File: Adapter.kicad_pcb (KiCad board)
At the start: 6 copper layers, 189.7 x 92 mm, 291 parts, among them J1 GD820HTX75P6HB, J2 2-338069-0, U1 R-78E3.3-1.0, U10 74LVC1G04, U11 LMV7219M5, U2 LM1117GS-3.3, U4 74LVC1G04, U5 ADuM1200AR, U6 74LVC1G04, U7 74LVC1G04, U8 74LVC1G04, U9 74LVC1G04

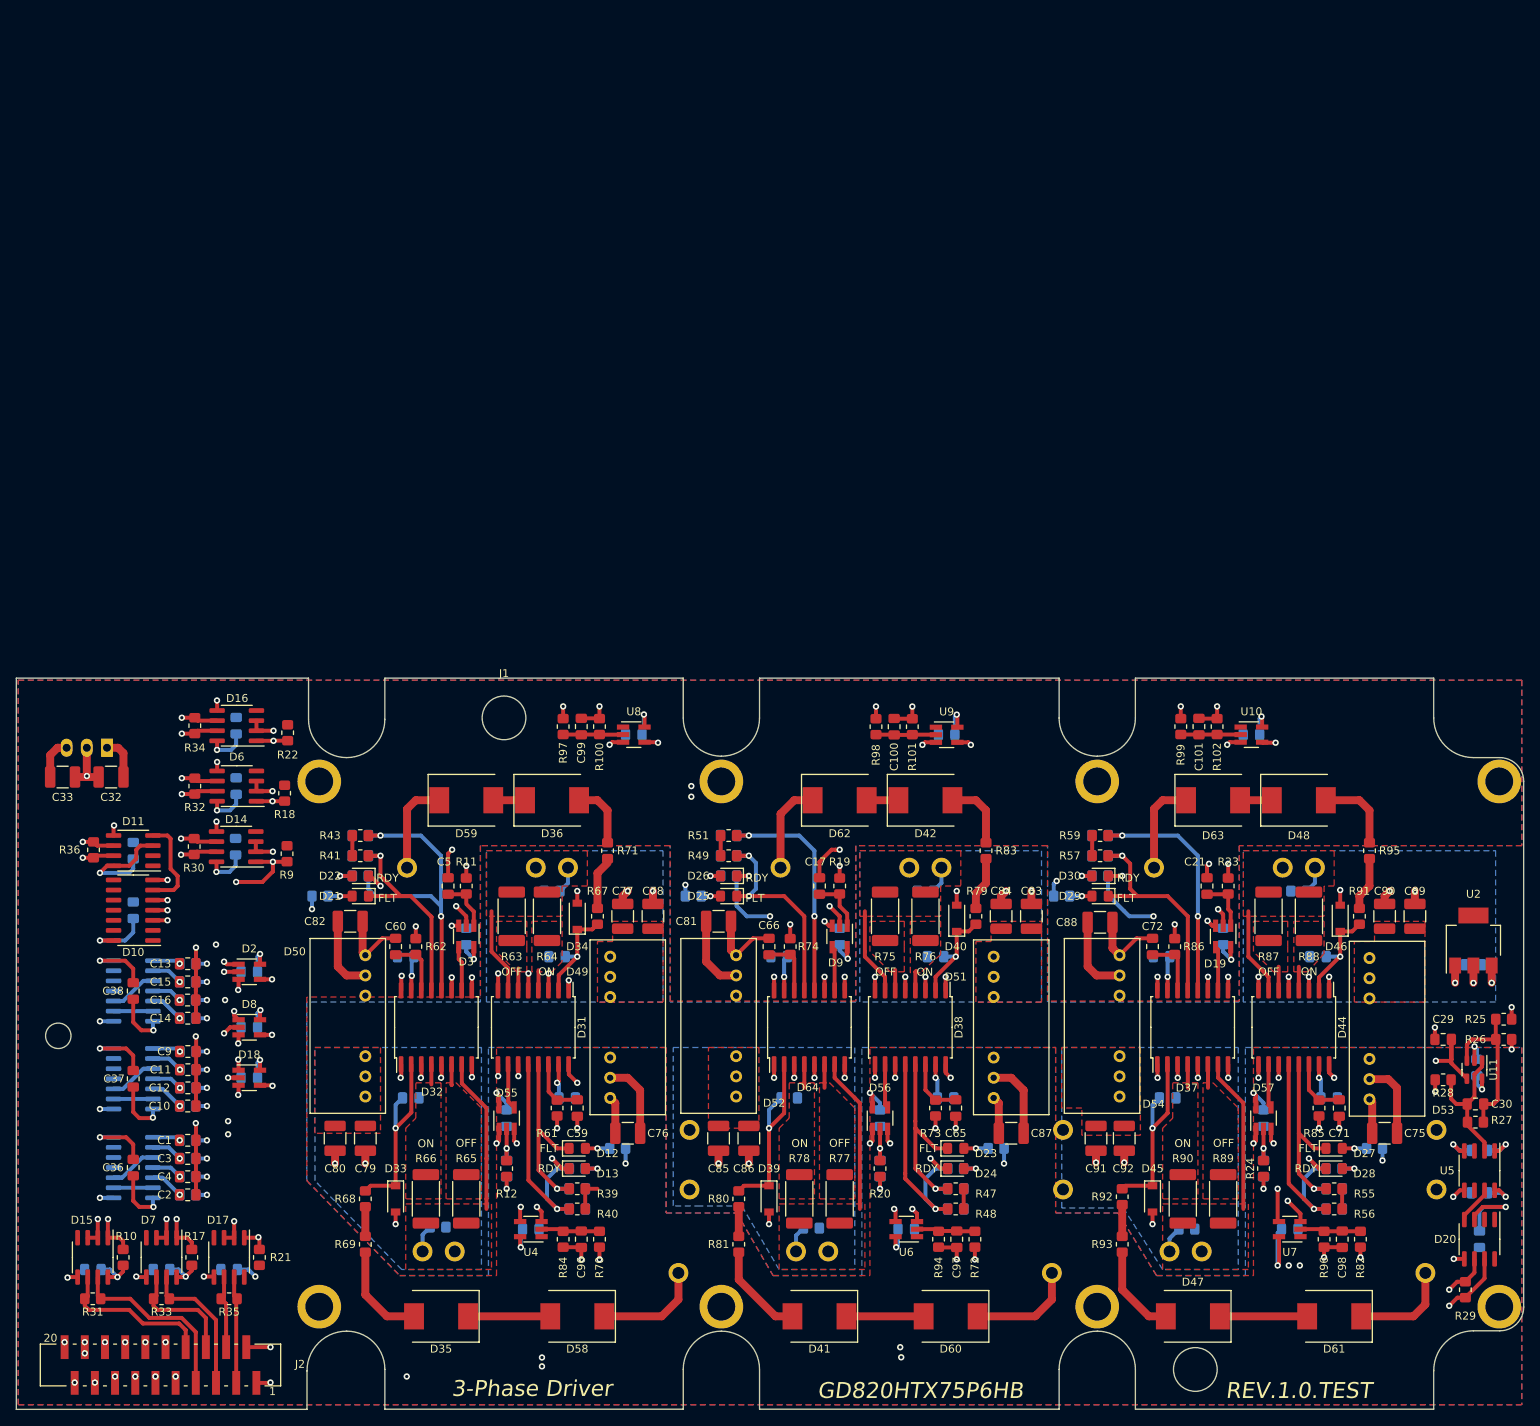
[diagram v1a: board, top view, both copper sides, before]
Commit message: Изменил схему
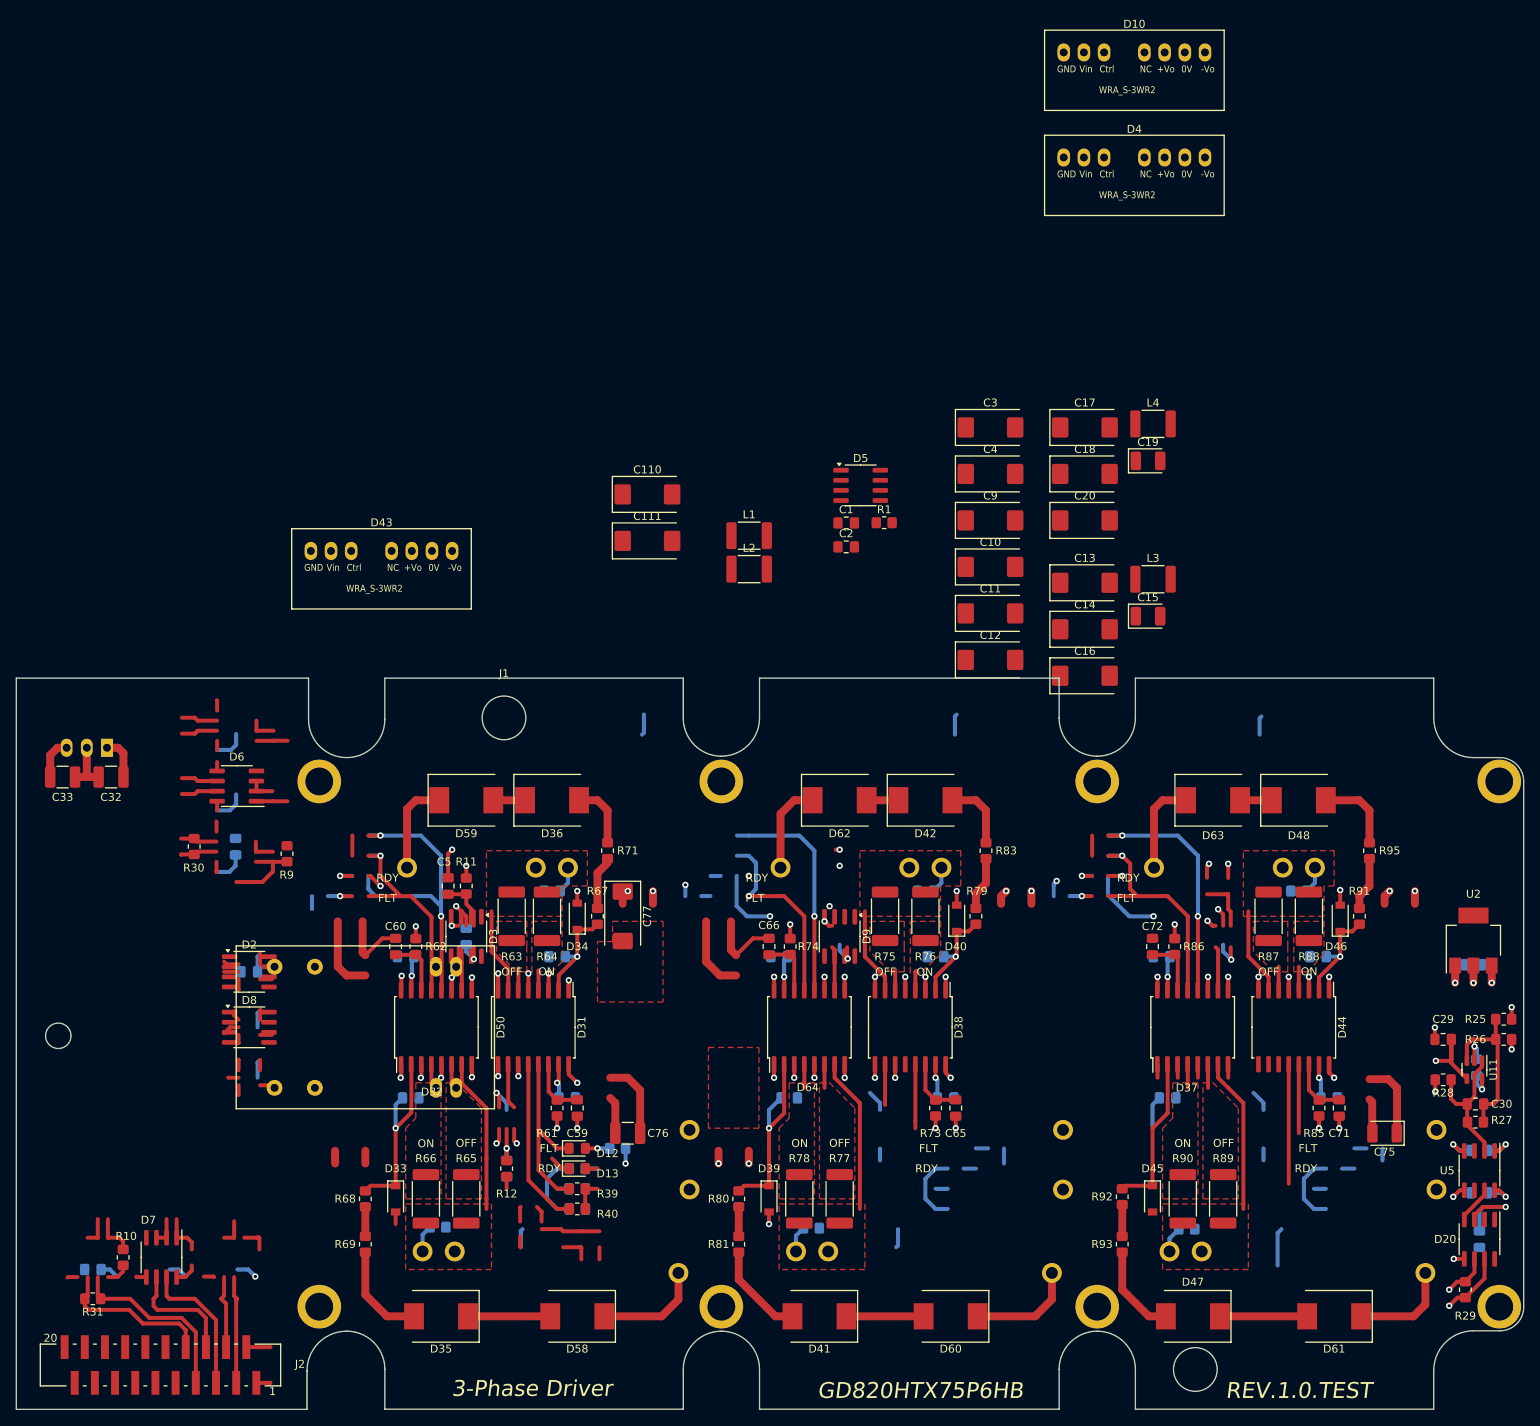
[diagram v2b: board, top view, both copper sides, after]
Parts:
- removed C100, C101, C21, C22, C47, C48, C49, C50, C51, C52, C53, C54, C55, C56, C96, C97, C98, C99: 56p, Capacitor_SMD:C_0805_2012Metric_Pad1.18x1.45mm_HandSolder
- removed C102, C103, C104, C105, C106, C107, C23, C24, C25, C26, C31, C36, C37, C38, C39, C43, C44, C93, C94, C95: 2.2u, Capacitor_SMD:C_0805_2012Metric_Pad1.18x1.45mm_HandSolder
- removed C78, C79, C80, C81, C82, C83, C84, C85, C86, C87, C88, C89, C90, C91, C92: 10u, Capacitor_SMD:C_1210_3225Metric_Pad1.33x2.70mm_HandSolder
- removed D1: SN74AC08DR, Package_SO:SOIC-14_3.9x8.7mm_P1.27mm
- removed D11, D14, D15, D16, D17: ADM3485E, Package_SO:SOIC-8_3.9x4.9mm_P1.27mm
- removed D18: SN74AHC1G32DBVR, Package_TO_SOT_SMD:SOT-23-5_HandSoldering
- removed D19, D55, D56, D57: SN74AHC1G86DBVR, Package_TO_SOT_SMD:SOT-23-5_HandSoldering
- removed D21, D23, D25, D27, D29: FLT, LED_SMD:LED_0805_2012Metric_Pad1.15x1.40mm_HandSolder
- removed D22, D24, D26, D28, D30: RDY, LED_SMD:LED_0805_2012Metric_Pad1.15x1.40mm_HandSolder
- removed D49, D51, D52, D53, D54: WRA1215S-3WR2, Mornsun:WRA1215S-3WR2
- removed R100, R101, R102, R17, R18, R21, R22, R41, R47, R49, R55, R57, R84, R94, R96: 10k, Resistor_SMD:R_0805_2012Metric_Pad1.20x1.40mm_HandSolder
- removed R13, R14, R15, R16, R19, R2, R20, R23, R24, R3, R32, R33, R34, R35, R36, R4, R43, R48, R5, R51, R56, R59, R6, R7, R70, R72, R8, R82, R97, R98, R99: 120, Resistor_SMD:R_0805_2012Metric_Pad1.20x1.40mm_HandSolder
- removed R42, R44, R45, R46, R50, R52, R53, R54, R58, R60: 330, Resistor_SMD:R_0805_2012Metric_Pad1.20x1.40mm_HandSolder
- removed U10, U4, U6, U7, U8, U9: 74LVC1G04, Package_TO_SOT_SMD:SOT-23-5_HandSoldering
- added C110: 10u, Capacitor_Tantalum_SMD:CP_EIA-7343-31_Kemet-D, F.Cu at (118.0, 24.4)
- added C111: 47u, Capacitor_Tantalum_SMD:CP_EIA-7343-31_Kemet-D, F.Cu at (118.0, 30.2)
- added D43: WRA1215S-3WR2, Mornsun:WRA_S-3WR2, F.Cu at (84.6, 31.5)
- added L1: 4.7u, Inductor_SMD:L_1812_4532Metric_Pad1.30x3.40mm_HandSolder, F.Cu at (130.8, 29.6)
- added L2: 4.7u, Inductor_SMD:L_1812_4532Metric_Pad1.30x3.40mm_HandSolder, F.Cu at (130.8, 33.8)
- added L3: 4.7u, Inductor_SMD:L_1812_4532Metric_Pad1.30x3.40mm_HandSolder, F.Cu at (181.7, 35.1)
- added L4: 4.7u, Inductor_SMD:L_1812_4532Metric_Pad1.30x3.40mm_HandSolder, F.Cu at (181.7, 15.5)
- C1, C2, C5, C6: value 56p -> 2.2u
- C10, C11, C12, C13, C16, C17, C3, C4, C9: value 56p -> 47u; footprint Capacitor_SMD:C_0805_2012Metric_Pad1.18x1.45mm_HandSolder -> Capacitor_Tantalum_SMD:CP_EIA-7343-31_Kemet-D
- C14: value 56p -> 10u; footprint Capacitor_SMD:C_0805_2012Metric_Pad1.18x1.45mm_HandSolder -> Capacitor_Tantalum_SMD:CP_EIA-7343-31_Kemet-D
- C15: value 56p -> 1u; footprint Capacitor_SMD:C_0805_2012Metric_Pad1.18x1.45mm_HandSolder -> Capacitor_Tantalum_SMD:CP_EIA-3528-21_Kemet-B
- C18: value 56p -> 10u; footprint Capacitor_SMD:C_0805_2012Metric_Pad1.18x1.45mm_HandSolder -> Capacitor_Tantalum_SMD:CP_EIA-7343-31_Kemet-D; moved to F.Cu
- C19: value 2.2u -> 1u; footprint Capacitor_SMD:C_0805_2012Metric_Pad1.18x1.45mm_HandSolder -> Capacitor_Tantalum_SMD:CP_EIA-3528-21_Kemet-B; moved to F.Cu
- C20: value 2.2u -> 47u; footprint Capacitor_SMD:C_0805_2012Metric_Pad1.18x1.45mm_HandSolder -> Capacitor_Tantalum_SMD:CP_EIA-7343-31_Kemet-D; moved to F.Cu
- C75: value 10u -> 1u; footprint Capacitor_SMD:C_1210_3225Metric_Pad1.33x2.70mm_HandSolder -> Capacitor_Tantalum_SMD:CP_EIA-3528-21_Kemet-B
- C76: value 10u -> 1u
- C77: value 10u -> 47u; footprint Capacitor_SMD:C_1210_3225Metric_Pad1.33x2.70mm_HandSolder -> Capacitor_Tantalum_SMD:CP_EIA-7343-31_Kemet-D
- D10: value SN74HC11DR -> WRA1215S-3WR2; footprint Package_SO:SOIC-14_3.9x8.7mm_P1.27mm -> Mornsun:WRA_S-3WR2
- D2, D8: value SN74AHC1G32DBVR -> ADM3485E; footprint Package_TO_SOT_SMD:SOT-23-5_HandSoldering -> Package_SO:SOIC-8_3.9x4.9mm_P1.27mm
- D3, D9: value SN74AHC1G86DBVR -> ADM3485E; footprint Package_TO_SOT_SMD:SOT-23-5_HandSoldering -> Package_SO:SOIC-8_3.9x4.9mm_P1.27mm
- D4: value SN74AC08DR -> WRA1215S-3WR2; footprint Package_SO:SOIC-14_3.9x8.7mm_P1.27mm -> Mornsun:WRA_S-3WR2; moved to F.Cu
- D5: value SN74AC08DR -> ADM3485E; footprint Package_SO:SOIC-14_3.9x8.7mm_P1.27mm -> Package_SO:SOIC-8_3.9x4.9mm_P1.27mm; moved to F.Cu
- D50: value WRA1215S-3WR2 -> URA2415ZP-6WR3; footprint Mornsun:WRA1215S-3WR2 -> Mornsun:URA_ZP-6WR3
- R1: moved to F.Cu
- R10, R9: value 10k -> 120
- R39: value 10k -> 30k
- R40: value 120 -> 30k
- moved D4 171.2 mm to (179.3, -18.0), turned to 0 degrees
- moved D10 165.9 mm to (179.3, -31.2), turned to 0 degrees
- moved C3 136.6 mm to (161.2, 16.0)
- moved C4 134.3 mm to (161.2, 21.8)
- moved C15 129.3 mm to (181.0, 39.7)
- moved C14 123.1 mm to (173.1, 41.4)
- moved C20 123.0 mm to (173.1, 27.7), turned to 0 degrees
- moved C13 122.7 mm to (173.1, 35.5)
- moved C10 121.7 mm to (161.2, 33.5)
- moved C9 121.1 mm to (161.2, 27.7)
- moved C16 120.1 mm to (173.1, 47.2)
- moved R1 117.1 mm to (147.8, 27.9)
- moved C2 116.3 mm to (143.1, 31.0)
- moved C11 116.2 mm to (161.2, 39.4)
- moved C12 114.5 mm to (161.2, 45.2)
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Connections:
- C1 pad 1: Net-(D1-1A) -> +3V3
- C10 pad 1: Net-(D4-2B) -> E4
- C10 pad 2: GND -> -15V_L1
- C11 pad 1: Net-(D4-1B) -> +15V_L1
- C11 pad 2: GND -> E6
- C12 pad 1: Net-(D4-2A) -> E6
- C12 pad 2: GND -> -15V_L1
- C13 pad 1: Net-(D5-1A) -> +15V_H2
- C13 pad 2: GND -> E3
- C14 pad 1: Net-(D5-2B) -> +15V
- C15 pad 1: Net-(D5-1B) -> Net-(D4-Vin)
- C16 pad 1: Net-(D5-2A) -> E3
- C16 pad 2: GND -> -15V_H2
- C17 pad 1: Net-(D9-A) -> +15V_H3
- C17 pad 2: GND -> E5
- C18 pad 1: Net-(D56-B) -> +15V
- C19 pad 1: +3V3 -> Net-(D10-Vin)
- C2 pad 1: Net-(D1-2B) -> +3V3
- C20 pad 1: +3V3 -> E5
- C20 pad 2: GND -> -15V_H3
- C27 pad 2: -15V_L3 -> -15V_L1
- C28 pad 2: -15V_L3 -> -15V_L1
- C29 pad 2: -15V_L3 -> -15V_L1
- C3 pad 1: Net-(D1-1B) -> +15V_L1
- C3 pad 2: GND -> E2
- C4 pad 1: Net-(D1-2A) -> E2
- C4 pad 2: GND -> -15V_L1
- C40 pad 2: -15V_L3 -> -15V_L1
- C45 pad 1: FLT_L1 -> FLT
- C46 pad 1: RDY_L1 -> RDY
- C5 pad 1: Net-(D3-A) -> +3V3
- C6 pad 1: Net-(D55-B) -> +3V3
- C75 pad 1: +15V -> Net-(D43-Vin)
- C77 pad 1: +15V_L1 -> E1
- C77 pad 2: E2 -> -15V_H1
- C9 pad 1: Net-(D4-1A) -> +15V_L1
- C9 pad 2: GND -> E4
- D10 pad 1: unconnected-(D10-1A-Pad1) -> GND
- D10 pad 2: unconnected-(D10-1B-Pad2) -> Net-(D10-Vin)
- D10 pad 3: FAULT_1 -> unconnected-(D10-Ctrl-Pad3)
- D10 pad 5: FAULT_3 -> (no net)
- D10 pad 6: FAULT_COMM -> +15V_H3
- D10 pad 7: GND -> E5
- D10 pad 8: unconnected-(D10-3Y-Pad8) -> -15V_H3
- D12 pad 1: FLT_L1 -> FLT
- D2 pad 1: Net-(D14-RO) -> PWM_H1
- D2 pad 2: Net-(D15-RO) -> GND
- D2 pad 4: Net-(D2-Y) -> unconnected-(D2-DI-Pad4)
- D2 pad 5: +3V3 -> GND
- D3 pad 1: Net-(D3-A) -> PWM_L1
- D3 pad 2: Net-(D2-Y) -> GND
- D3 pad 4: PWM_H1 -> unconnected-(D3-DI-Pad4)
- D3 pad 5: +3V3 -> GND
- D31 pad 11: GND -> PWM_H1
- D32 pad 11: GND -> PWM_L1
- D37 pad 11: GND -> PWM_L3
- D38 pad 1: -15V_L2 -> -15V_L1
- D38 pad 11: GND -> PWM_H2
- D38 pad 5: +15V_L2 -> +15V_L1
- D38 pad 8: -15V_L2 -> -15V_L1
- D4 pad 1: Net-(D4-1A) -> GND
- D4 pad 2: Net-(D4-1B) -> Net-(D4-Vin)
- D4 pad 3: /Fault2/FLT -> unconnected-(D4-Ctrl-Pad3)
- D4 pad 5: Net-(D4-2B) -> (no net)
- D4 pad 6: /Fault2/RDY -> +15V_H2
- D4 pad 7: GND -> E3
- D4 pad 8: FAULT_2 -> -15V_H2
- D44 pad 1: -15V_L3 -> -15V_L1
- D44 pad 11: GND -> PWM_H3
- D44 pad 5: +15V_L3 -> +15V_L1
- D44 pad 8: -15V_L3 -> -15V_L1
- D5 pad 1: Net-(D5-1A) -> unconnected-(D5-RO-Pad1)
- D5 pad 2: Net-(D5-1B) -> +3V3
- D5 pad 3: /Fault3/FLT -> +3V3
- D5 pad 4: Net-(D5-2A) -> Net-(D1-Y)
- D5 pad 5: Net-(D5-2B) -> GND
- D5 pad 6: /Fault3/RDY -> ERR_P
- D5 pad 7: GND -> ERR_N
- D5 pad 8: FAULT_3 -> +3V3
- D50 pad 2: +15V -> GND
- D50 pad 3: unconnected-(D50-Ctrl-Pad3) -> GND
- D6 pad 1: Net-(D6-RO) -> PWM_L3
- D6 pad 6: PWM2_L_P -> PWM3_L_P
- D6 pad 7: PWM2_L_N -> PWM3_L_N
- D64 pad 11: GND -> PWM_L2
- D7 pad 1: Net-(D7-RO) -> PWM_H3
- D7 pad 6: PWM2_H_P -> PWM3_H_P
- D7 pad 7: PWM2_H_N -> PWM3_H_N
- D8 pad 1: Net-(D6-RO) -> PWM_L2
- D8 pad 2: Net-(D7-RO) -> GND
- D8 pad 4: Net-(D56-A) -> unconnected-(D8-DI-Pad4)
- D8 pad 5: +3V3 -> GND
- D9 pad 1: Net-(D9-A) -> PWM_H2
- D9 pad 2: Net-(D56-A) -> GND
- D9 pad 4: PWM_H2 -> unconnected-(D9-DI-Pad4)
- D9 pad 5: +3V3 -> GND
- J2 pad 20: Reset -> unconnected-(J2-Pad20)
- R1 pad 1: Net-(D1-1A) -> ERR_N
- R1 pad 2: FLT_H1 -> ERR_P
- R10 pad 1: +3V3 -> PWM2_H_N
- R10 pad 2: Net-(D15-RO) -> PWM2_H_P
- R11 pad 1: Net-(D14-RO) -> PWM3_L_N
- R11 pad 2: Net-(D3-A) -> PWM3_L_P
- R12 pad 1: Net-(D15-RO) -> PWM3_H_N
- R12 pad 2: Net-(D55-B) -> PWM3_H_P
- R26 pad 1: -15V_L3 -> -15V_L1
- R38 pad 2: RDY_L1 -> RDY
- R39 pad 1: FLT_L1 -> FLT
- R40 pad 1: RDY_L1 -> RDY
- R61 pad 1: RST_L1 -> PWM_L1
- R62 pad 1: RST_H1 -> PWM_H1
- R73 pad 1: RST_L2 -> PWM_L2
- R74 pad 1: RST_H2 -> PWM_H2
- R85 pad 1: RST_L3 -> PWM_L3
- R86 pad 1: RST_H3 -> PWM_H3
- R9 pad 1: +3V3 -> PWM2_L_N
- R9 pad 2: Net-(D14-RO) -> PWM2_L_P
- U11 pad 2: -15V_L3 -> -15V_L1
- U2 pad 1: -15V_L3 -> -15V_L1
- U5 pad 4: -15V_L3 -> -15V_L1
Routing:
- net (no net): track 0.00 -> 657.1 mm, vias 0 -> 9
- net Reset: track 413.3 -> 0.00 mm, vias 7 -> 0
- net unconnected-(J2-Pad20): track 0.00 -> 405.8 mm
- net Net-(D18-Y): track 348.2 -> 0.00 mm, vias 3 -> 0
- net Net-(D56-A): track 223.4 -> 0.00 mm, vias 3 -> 0
- net Net-(D17-RO): track 177.7 -> 0.00 mm, vias 3 -> 0
- net Net-(D16-RO): track 177.4 -> 0.00 mm, vias 3 -> 0
- net Net-(D7-RO): track 152.9 -> 0.00 mm, vias 3 -> 0
- net PWM2_L_P: track 82.6 -> 228.7 mm, vias 2 -> 1
- net Net-(D6-RO): track 114.1 -> 0.00 mm, vias 3 -> 0
- net GND: track 239.9 -> 129.4 mm, vias 76 -> 26
- net Net-(D2-Y): track 109.9 -> 0.00 mm, vias 3 -> 0
- net Net-(D15-RO): track 107.2 -> 0.00 mm, vias 3 -> 0
- net PWM3_H_N: track 13.5 -> 113.4 mm
- net PWM_L3: track 5.56 -> 95.9 mm, vias 0 -> 3
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- added copper zone on In2.Cu, net -15V_L1
- removed copper zone on In1.Cu, net +15V
- removed copper zone on In3.Cu, net +15V_H1
- removed copper zone on In3.Cu, net +15V_H2
- removed copper zone on In3.Cu, net +15V_H3
- removed copper zone on In3.Cu, net +15V_L1
- removed copper zone on In3.Cu, net +15V_L2
- removed copper zone on In3.Cu, net +15V_L3
- removed copper zone on F.Cu, net +3V3
- removed copper zone on In4.Cu, net -15V_H1
- removed copper zone on In4.Cu, net -15V_H2
- removed copper zone on In4.Cu, net -15V_H3
- removed copper zone on In4.Cu, net -15V_L1
- removed copper zone on In4.Cu, net -15V_L2
- removed copper zone on In2.Cu, net -15V_L3
- removed copper zone on In4.Cu, net -15V_L3
- removed copper zone on B.Cu, net E1
- removed copper zone on F.Cu, net E1
- removed copper zone on B.Cu, net E2
- removed copper zone on B.Cu, net E3
- removed copper zone on B.Cu, net E4
- removed copper zone on F.Cu, net E4
- removed copper zone on B.Cu, net E5
- removed copper zone on F.Cu, net E5
- removed copper zone on B.Cu, net E6
- removed copper zone on F.Cu, net E6
- removed copper zone on B.Cu, net GND

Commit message: Разместил все три стойки в своей области
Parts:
- removed C110: 10u, Capacitor_Tantalum_SMD:CP_EIA-7343-31_Kemet-D
- removed C111, C77: 47u, Capacitor_Tantalum_SMD:CP_EIA-7343-31_Kemet-D
- removed C75: 1u, Capacitor_Tantalum_SMD:CP_EIA-3528-21_Kemet-B
- removed C76: 1u, Capacitor_SMD:C_1210_3225Metric_Pad1.33x2.70mm_HandSolder
- removed D50: URA2415ZP-6WR3, Mornsun:URA_ZP-6WR3
- removed H1: MountingHole, MountingHole:MountingHole_3.2mm_M3
- removed R63, R64, R65, R75, R76, R77, R78, R87, R88, R89, R90: 3, Resistor_SMD:R_2512_6332Metric_Pad1.40x3.35mm_HandSolder
- added C21: 0.1u, Capacitor_SMD:C_0805_2012Metric_Pad1.18x1.45mm_HandSolder, F.Cu at (-4.57, 68.0)
- added C22: 10u, Capacitor_SMD:C_0805_2012Metric_Pad1.18x1.45mm_HandSolder, F.Cu at (-4.57, 71.0)
- added C23: 0.1u, Capacitor_SMD:C_0805_2012Metric_Pad1.18x1.45mm_HandSolder, F.Cu at (-4.57, 74.0)
- added C24: 10u, Capacitor_SMD:C_0805_2012Metric_Pad1.18x1.45mm_HandSolder, F.Cu at (-4.57, 77.0)
- added C25: 0.1u, Capacitor_SMD:C_0805_2012Metric_Pad1.18x1.45mm_HandSolder, F.Cu at (-4.57, 80.0)
- added C26: 10u, Capacitor_SMD:C_0805_2012Metric_Pad1.18x1.45mm_HandSolder, F.Cu at (-4.57, 83.0)
- added C31: 10u, Capacitor_SMD:C_1210_3225Metric_Pad1.33x2.70mm_HandSolder, F.Cu at (93.5, 104.4)
- added C36: 10u, Capacitor_SMD:C_1210_3225Metric_Pad1.33x2.70mm_HandSolder, F.Cu at (88.4, 104.4)
- added C37: 10u, Capacitor_SMD:C_1210_3225Metric_Pad1.33x2.70mm_HandSolder, F.Cu at (88.9, 77.0)
- added C38: 10u, Capacitor_SMD:C_1210_3225Metric_Pad1.33x2.70mm_HandSolder, F.Cu at (92.5, 77.0)
- added C39: 10u, Capacitor_SMD:C_1210_3225Metric_Pad1.33x2.70mm_HandSolder, F.Cu at (156.0, 115.3)
- added C43: 10u, Capacitor_SMD:C_1210_3225Metric_Pad1.33x2.70mm_HandSolder, F.Cu at (156.2, 86.6)
- added C44: 10u, Capacitor_SMD:C_1210_3225Metric_Pad1.33x2.70mm_HandSolder, F.Cu at (198.1, 86.6)
- added C47: 10u, Capacitor_SMD:C_1210_3225Metric_Pad1.33x2.70mm_HandSolder, F.Cu at (199.4, 115.3)
- added C48: 10u, Capacitor_SMD:C_1210_3225Metric_Pad1.33x2.70mm_HandSolder, F.Cu at (202.9, 115.3)
- added C49: 10u, Capacitor_SMD:C_1210_3225Metric_Pad1.33x2.70mm_HandSolder, F.Cu at (203.2, 86.6)
- added D11: ~, Sensors_My:YMC15S-500A, F.Cu at (202.3, 150.7)
- added D14: ~, Sensors_My:YMC15S-500A, F.Cu at (155.3, 150.7)
- added D15: ~, Sensors_My:YMC15S-500A, F.Cu at (108.3, 150.8)
- added D16: WRA1215S-3WR2, Mornsun:WRA_S-3WR2, F.Cu at (113.5, 107.4)
- added D17: WRA1215S-3WR2, Mornsun:WRA_S-3WR2, F.Cu at (160.5, 107.4)
- added D18: WRA1215S-3WR2, Mornsun:WRA_S-3WR2, F.Cu at (207.6, 107.4)
- added D19: PWR, LED_SMD:LED_0805_2012Metric_Pad1.15x1.40mm_HandSolder, F.Cu at (234.7, 67.3)
- added L5: 4.7u, Inductor_SMD:L_1812_4532Metric_Pad1.30x3.40mm_HandSolder, F.Cu at (154.2, 110.7)
- added L6: 4.7u, Inductor_SMD:L_1812_4532Metric_Pad1.30x3.40mm_HandSolder, F.Cu at (201.2, 110.7)
- added R13: 10, Resistor_SMD:R_1206_3216Metric_Pad1.30x1.75mm_HandSolder, F.Cu at (89.6, 115.3)
- added R14: 10, Resistor_SMD:R_1206_3216Metric_Pad1.30x1.75mm_HandSolder, F.Cu at (121.7, 75.7)
- added R15: 10, Resistor_SMD:R_1206_3216Metric_Pad1.30x1.75mm_HandSolder, F.Cu at (109.0, 75.7)
- added R16: 10, Resistor_SMD:R_1206_3216Metric_Pad1.30x1.75mm_HandSolder, F.Cu at (111.5, 75.7)
- added R17: 10, Resistor_SMD:R_1206_3216Metric_Pad1.30x1.75mm_HandSolder, F.Cu at (114.0, 75.7)
- added R18: 10, Resistor_SMD:R_1206_3216Metric_Pad1.30x1.75mm_HandSolder, F.Cu at (116.6, 75.7)
- added R19: 10, Resistor_SMD:R_1206_3216Metric_Pad1.30x1.75mm_HandSolder, F.Cu at (119.1, 75.7)
- added R2: 0, Resistor_SMD:R_0805_2012Metric_Pad1.20x1.40mm_HandSolder, F.Cu at (-4.60, 86.0)
- added R20: 10, Resistor_SMD:R_1206_3216Metric_Pad1.30x1.75mm_HandSolder, F.Cu at (131.3, 115.3)
- added R21: 10, Resistor_SMD:R_1206_3216Metric_Pad1.30x1.75mm_HandSolder, F.Cu at (128.8, 115.3)
- added R22: 10, Resistor_SMD:R_1206_3216Metric_Pad1.30x1.75mm_HandSolder, F.Cu at (136.4, 115.3)
- added R23: 10, Resistor_SMD:R_1206_3216Metric_Pad1.30x1.75mm_HandSolder, F.Cu at (168.7, 75.7)
- added R24: 10, Resistor_SMD:R_1206_3216Metric_Pad1.30x1.75mm_HandSolder, F.Cu at (156.0, 75.7)
- added R3: 0, Resistor_SMD:R_0805_2012Metric_Pad1.20x1.40mm_HandSolder, F.Cu at (-4.60, 89.0)
- added R32: 10, Resistor_SMD:R_1206_3216Metric_Pad1.30x1.75mm_HandSolder, F.Cu at (166.1, 75.7)
- added R33: 10, Resistor_SMD:R_1206_3216Metric_Pad1.30x1.75mm_HandSolder, F.Cu at (173.2, 115.3)
- added R34: 10, Resistor_SMD:R_1206_3216Metric_Pad1.30x1.75mm_HandSolder, F.Cu at (175.8, 115.3)
- added R35: 10, Resistor_SMD:R_1206_3216Metric_Pad1.30x1.75mm_HandSolder, F.Cu at (178.3, 115.3)
- added R36: 10, Resistor_SMD:R_1206_3216Metric_Pad1.30x1.75mm_HandSolder, F.Cu at (215.6, 75.7)
- added R4: 0, Resistor_SMD:R_0805_2012Metric_Pad1.20x1.40mm_HandSolder, F.Cu at (-4.60, 91.9)
- added R41: 10, Resistor_SMD:R_1206_3216Metric_Pad1.30x1.75mm_HandSolder, F.Cu at (202.9, 75.7)
- added R42: 10, Resistor_SMD:R_1206_3216Metric_Pad1.30x1.75mm_HandSolder, F.Cu at (205.5, 75.7)
- added R43: 10, Resistor_SMD:R_1206_3216Metric_Pad1.30x1.75mm_HandSolder, F.Cu at (138.9, 115.3)
- added R44: 10, Resistor_SMD:R_1206_3216Metric_Pad1.30x1.75mm_HandSolder, F.Cu at (126.2, 115.3)
- added R45: 10, Resistor_SMD:R_1206_3216Metric_Pad1.30x1.75mm_HandSolder, F.Cu at (133.9, 115.3)
- added R46: 10, Resistor_SMD:R_1206_3216Metric_Pad1.30x1.75mm_HandSolder, F.Cu at (183.4, 115.3)
- added R47: 10, Resistor_SMD:R_1206_3216Metric_Pad1.30x1.75mm_HandSolder, F.Cu at (185.9, 115.3)
- added R48: 10, Resistor_SMD:R_1206_3216Metric_Pad1.30x1.75mm_HandSolder, F.Cu at (180.8, 115.3)
- added R49: 10, Resistor_SMD:R_1206_3216Metric_Pad1.30x1.75mm_HandSolder, F.Cu at (163.6, 75.7)
- added R5: 10, Resistor_SMD:R_1206_3216Metric_Pad1.30x1.75mm_HandSolder, F.Cu at (79.5, 115.3)
- added R50: 10, Resistor_SMD:R_1206_3216Metric_Pad1.30x1.75mm_HandSolder, F.Cu at (161.0, 75.7)
- added R51: 10, Resistor_SMD:R_1206_3216Metric_Pad1.30x1.75mm_HandSolder, F.Cu at (158.5, 75.7)
- added R52: 10, Resistor_SMD:R_1206_3216Metric_Pad1.30x1.75mm_HandSolder, F.Cu at (208.0, 75.7)
- added R53: 10, Resistor_SMD:R_1206_3216Metric_Pad1.30x1.75mm_HandSolder, F.Cu at (210.6, 75.7)
- added R54: 10, Resistor_SMD:R_1206_3216Metric_Pad1.30x1.75mm_HandSolder, F.Cu at (213.1, 75.7)
- added R55: 1.5k, Resistor_SMD:R_0805_2012Metric_Pad1.20x1.40mm_HandSolder, B.Cu at (234.7, 67.3)
- added R6: 10, Resistor_SMD:R_1206_3216Metric_Pad1.30x1.75mm_HandSolder, F.Cu at (82.0, 115.3)
- added R7: 10, Resistor_SMD:R_1206_3216Metric_Pad1.30x1.75mm_HandSolder, F.Cu at (84.6, 115.3)
- added R8: 10, Resistor_SMD:R_1206_3216Metric_Pad1.30x1.75mm_HandSolder, F.Cu at (87.1, 115.3)
- C1, C5, D33, D34, D39, D40, D45, D46: moved to B.Cu
- C10, C11, C12, C13, C16, C17, C20, C3, C4, C9: value 47u -> 10u; footprint Capacitor_Tantalum_SMD:CP_EIA-7343-31_Kemet-D -> Capacitor_SMD:C_1210_3225Metric_Pad1.33x2.70mm_HandSolder
- C14, C18: footprint Capacitor_Tantalum_SMD:CP_EIA-7343-31_Kemet-D -> Capacitor_SMD:C_1210_3225Metric_Pad1.33x2.70mm_HandSolder
- C15, C19: value 1u -> 10u; footprint Capacitor_Tantalum_SMD:CP_EIA-3528-21_Kemet-B -> Capacitor_SMD:C_1210_3225Metric_Pad1.33x2.70mm_HandSolder
- C45, C46, C57, C58, C63, C64, C69, C70, U1: moved to F.Cu
- D35, D36, D41, D42, D47, D48, D58, D59, D60, D61, D62, D63: footprint Diode_SMD:D_SMC -> Diode_SMD:D_SMA_Handsoldering
- R66: value 3 -> 10; footprint Resistor_SMD:R_2512_6332Metric_Pad1.40x3.35mm_HandSolder -> Resistor_SMD:R_1206_3216Metric_Pad1.30x1.75mm_HandSolder
- moved C2 182.6 mm to (-35.9, 67.3)
- moved R39 175.9 mm to (-64.3, 82.5)
- moved R40 175.9 mm to (-64.3, 85.1)
- moved J2 168.0 mm to (230.9, 87.5), turned to -90 degrees
- moved D6 148.2 mm to (211.6, 90.7), turned to 90 degrees
- moved D13 129.6 mm to (231.9, 67.3), turned to 90 degrees
- moved R38 129.6 mm to (231.9, 67.3), turned to -90 degrees
- moved C45 128.9 mm to (-17.6, 89.0), turned to 180 degrees
- moved C46 128.9 mm to (-17.6, 91.6), turned to 180 degrees
- moved D12 126.2 mm to (229.1, 67.3), turned to 90 degrees
- moved R37 121.4 mm to (229.1, 67.3), turned to -90 degrees
- moved D7 120.1 mm to (175.3, 100.3)
- moved R11 116.9 mm to (211.6, 85.6), turned to 0 degrees
- moved C7 116.8 mm to (211.6, 90.7), turned to 0 degrees
- moved D10 115.1 mm to (178.1, 83.8), turned to -90 degrees
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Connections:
- C10 pad 1: E4 -> E2
- C11 pad 1: +15V_L1 -> +15V_H2
- C11 pad 2: E6 -> E3
- C12 pad 1: E6 -> +15V
- C12 pad 2: -15V_L1 -> GND
- C13 pad 1: +15V_H2 -> Net-(D4-Vin)
- C13 pad 2: E3 -> GND
- C14 pad 1: +15V -> E3
- C14 pad 2: GND -> -15V_H2
- C15 pad 1: Net-(D4-Vin) -> +15V_L2
- C15 pad 2: GND -> E4
- C16 pad 1: E3 -> +15V
- C16 pad 2: -15V_H2 -> GND
- C27 pad 2: -15V_L1 -> -15V_L3
- C28 pad 2: -15V_L1 -> -15V_L3
- C29 pad 2: -15V_L1 -> -15V_L3
- C4 pad 1: E2 -> +15V
- C4 pad 2: -15V_L1 -> GND
- C40 pad 2: -15V_L1 -> -15V_L3
- C9 pad 1: +15V_L1 -> Net-(D16-Vin)
- C9 pad 2: E4 -> GND
- D38 pad 1: -15V_L1 -> -15V_L2
- D38 pad 5: +15V_L1 -> +15V_L2
- D38 pad 8: -15V_L1 -> -15V_L2
- D44 pad 1: -15V_L1 -> -15V_L3
- D44 pad 5: +15V_L1 -> +15V_L3
- D44 pad 8: -15V_L1 -> -15V_L3
- D5 pad 4: Net-(D1-Y) -> unconnected-(D5-DI-Pad4)
- L1 pad 2: Net-(C108-Pad1) -> Net-(D16-Vin)
- R26 pad 1: -15V_L1 -> -15V_L3
- U11 pad 2: -15V_L1 -> -15V_L3
- U2 pad 1: -15V_L1 -> -15V_L3
- U5 pad 4: -15V_L1 -> -15V_L3
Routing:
- net +3V3: track 139.2 -> 15.2 mm, vias 15 -> 2
- net RDY_H1: track 102.9 -> 0.00 mm, vias 2 -> 0
- net FLT_H1: track 80.2 -> 0.00 mm, vias 1 -> 0
- net (no net): track 657.1 -> 582.5 mm, vias 9 -> 0
- net RDY_H3: track 181.0 -> 140.7 mm, vias 3 -> 0
- net RDY_H2: track 111.0 -> 74.4 mm, vias 2 -> 0
- net FLT_H3: track 158.9 -> 129.1 mm, vias 1 -> 0
- net -15V_L1: track 29.3 -> 0.00 mm, vias 12 -> 0
- net -15V_L3: track 0.00 -> 25.7 mm, vias 0 -> 5
- net +15V: track 24.8 -> 0.00 mm
- net FLT_H2: track 108.5 -> 83.9 mm, vias 1 -> 0
- net Net-(D39-K): track 24.6 -> 0.00 mm, vias 1 -> 0
- net PWM2_H_N: track 24.5 -> 0.00 mm, vias 1 -> 0
- net Net-(D32-DESAT): track 24.4 -> 0.00 mm, vias 1 -> 0
- net Net-(D37-DESAT): track 24.2 -> 0.00 mm
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- removed copper zone on F.Cu, net E2
- removed copper zone on F.Cu, net E3
- removed copper zone on F.Cu, net G1
- removed copper zone on F.Cu, net G2
- removed copper zone on F.Cu, net G3
- removed copper zone on F.Cu, net G4
- removed copper zone on F.Cu, net G5
- removed copper zone on F.Cu, net G6
- removed copper zone on F.Cu, net Net-(D31-OUTH)
- removed copper zone on F.Cu, net Net-(D31-OUTL)
- removed copper zone on F.Cu, net Net-(D32-OUTH)
- removed copper zone on F.Cu, net Net-(D32-OUTL)
- removed copper zone on F.Cu, net Net-(D37-OUTH)
- removed copper zone on F.Cu, net Net-(D37-OUTL)
- removed copper zone on F.Cu, net Net-(D38-OUTH)
- removed copper zone on F.Cu, net Net-(D38-OUTL)
- removed copper zone on F.Cu, net Net-(D44-OUTH)
- removed copper zone on F.Cu, net Net-(D44-OUTL)
- removed copper zone on F.Cu, net Net-(D64-OUTH)
- removed copper zone on F.Cu, net Net-(D64-OUTL)
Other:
- board size 189.7 x 92 mm -> 164.7 x 117 mm
- board text removed: "FLT"
- board text removed: "OFF"
- board text removed: "ON"
- board text removed: "RDY"
